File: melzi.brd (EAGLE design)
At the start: 208.3 x 49.5 mm, 130 parts, among them IC2 A4988, IC3 A4988, IC4 A4988, IC5 7805DT, IC6 ATMEGA644A, IC7 4050D, IC8 FT232RL-BASICSSOP, M1 RFP30N06LE, M2 RFP30N06LE, M3 RFP30N06LE, Q1 16MHZ, T2 TRIM, T3 TRIM, T4 TRIM, U2 A4982, X1 MICROSD, X2 MINI-USB-SHIELD-UX60-MB-5ST

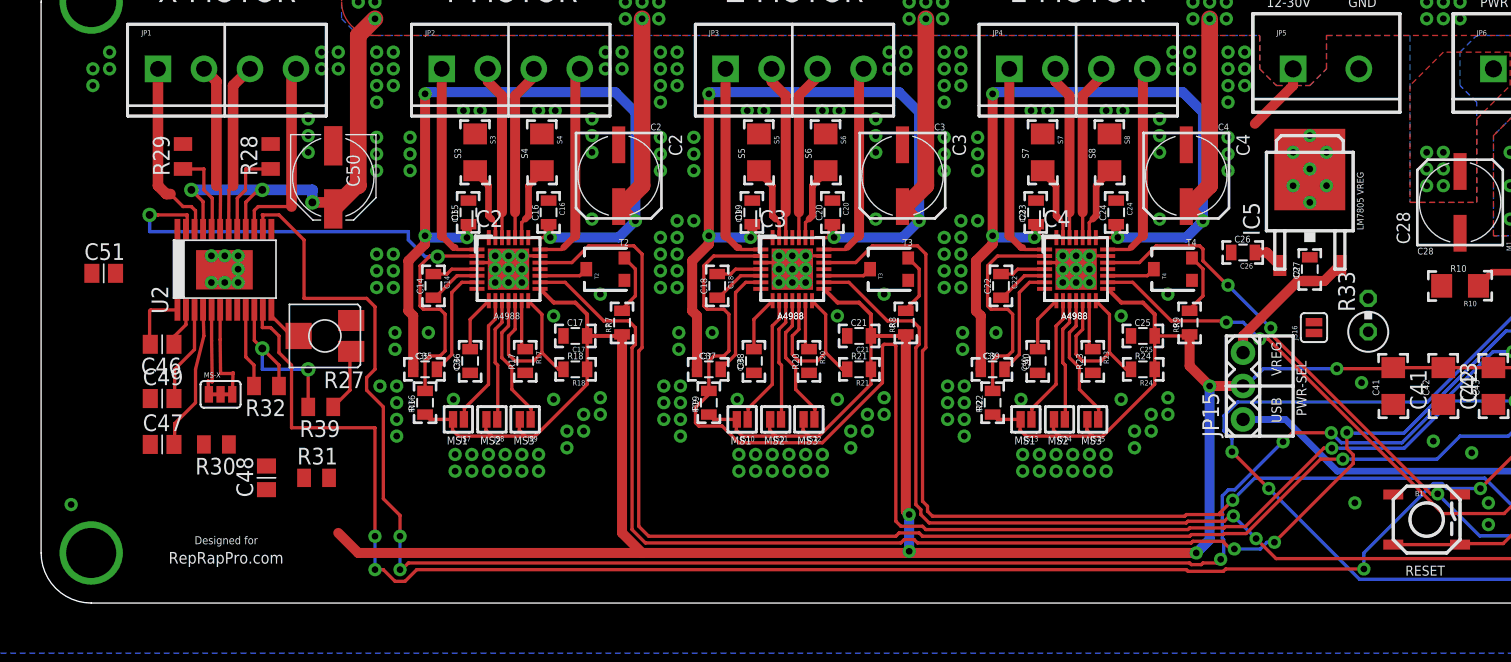
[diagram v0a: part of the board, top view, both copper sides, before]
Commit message: New stepper drivers - X axis done.
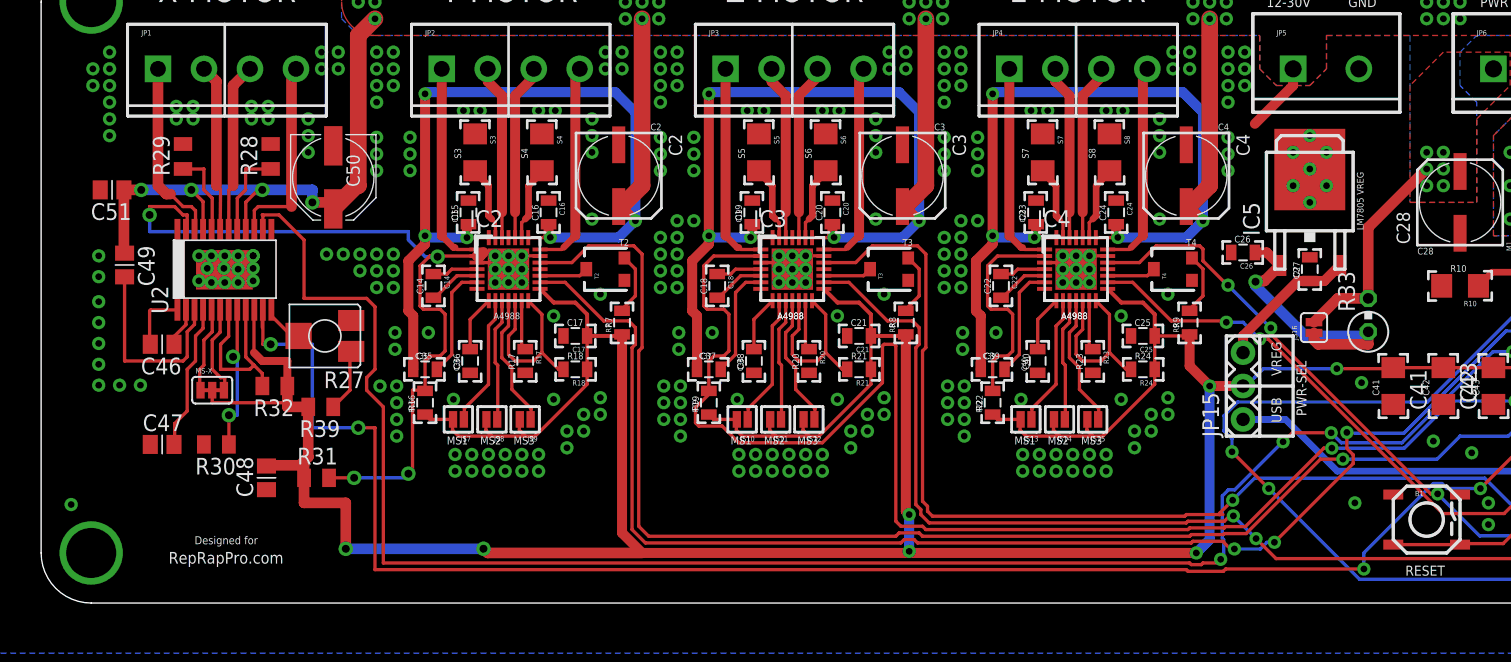
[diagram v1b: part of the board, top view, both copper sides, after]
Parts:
- moved C49 10.6 mm to (6.35, 25.7), turned to 270 degrees
- moved C51 6.38 mm to (5.40, 31.4), turned to 180 degrees
- moved MS-X 0.71 mm to (13.0, 16.2)
- moved R32 0.64 mm to (17.8, 16.5)
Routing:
- net VMOT: track 277.1 -> 303.6 mm, vias 95 -> 96
- net VCC: track 446.0 -> 465.4 mm
- net N$36: track 2.31 -> 21.1 mm, vias 0 -> 1
- net !XYEENABLE: track 62.6 -> 78.1 mm, vias 2 -> 4
- net N$8: track 0.00 -> 11.5 mm, vias 0 -> 2
- net N$10: track 6.05 -> 13.8 mm
- net N$23: track 7.39 -> 15.1 mm
- net X-STEP: track 136.2 -> 137.6 mm
- net N$31: track 7.51 -> 6.96 mm
- net X-DIR: vias 6 -> 4
- net GND: vias 300 -> 333

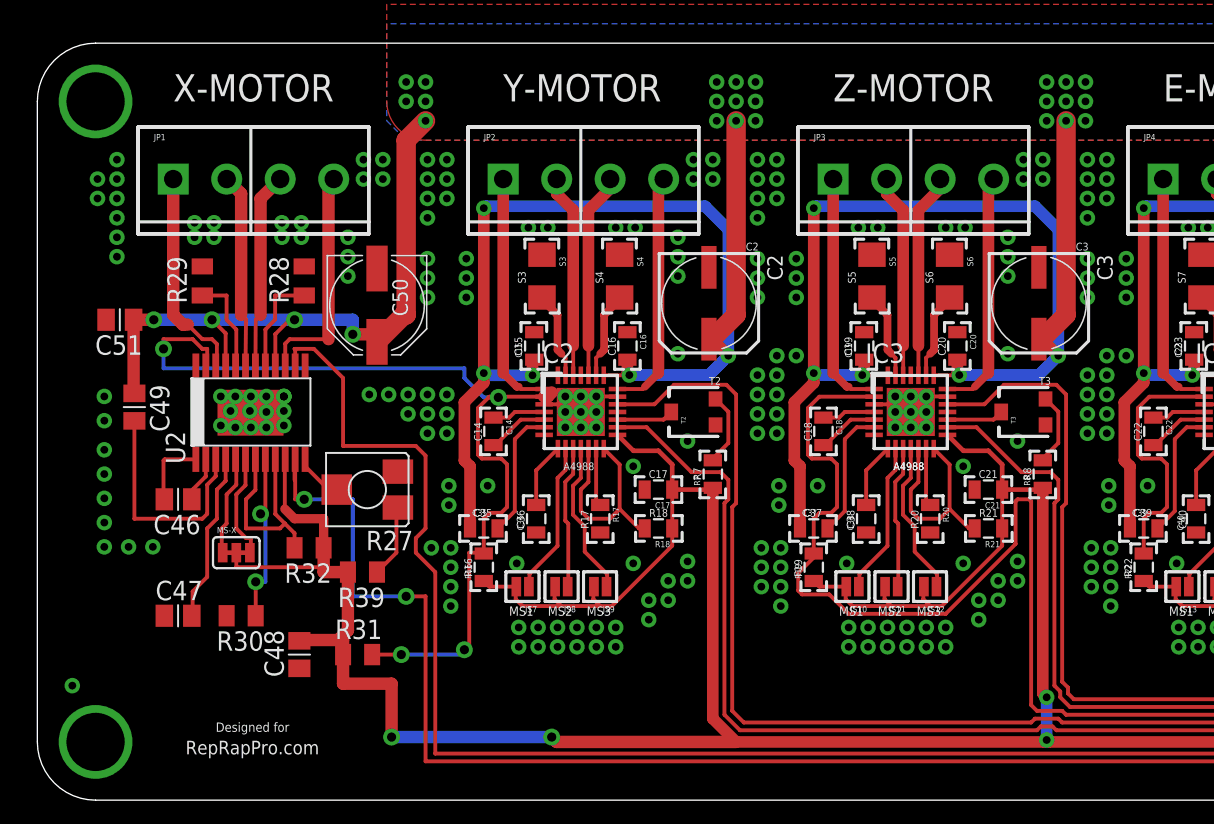
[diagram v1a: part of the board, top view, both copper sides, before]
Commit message: Y and Z drives added.
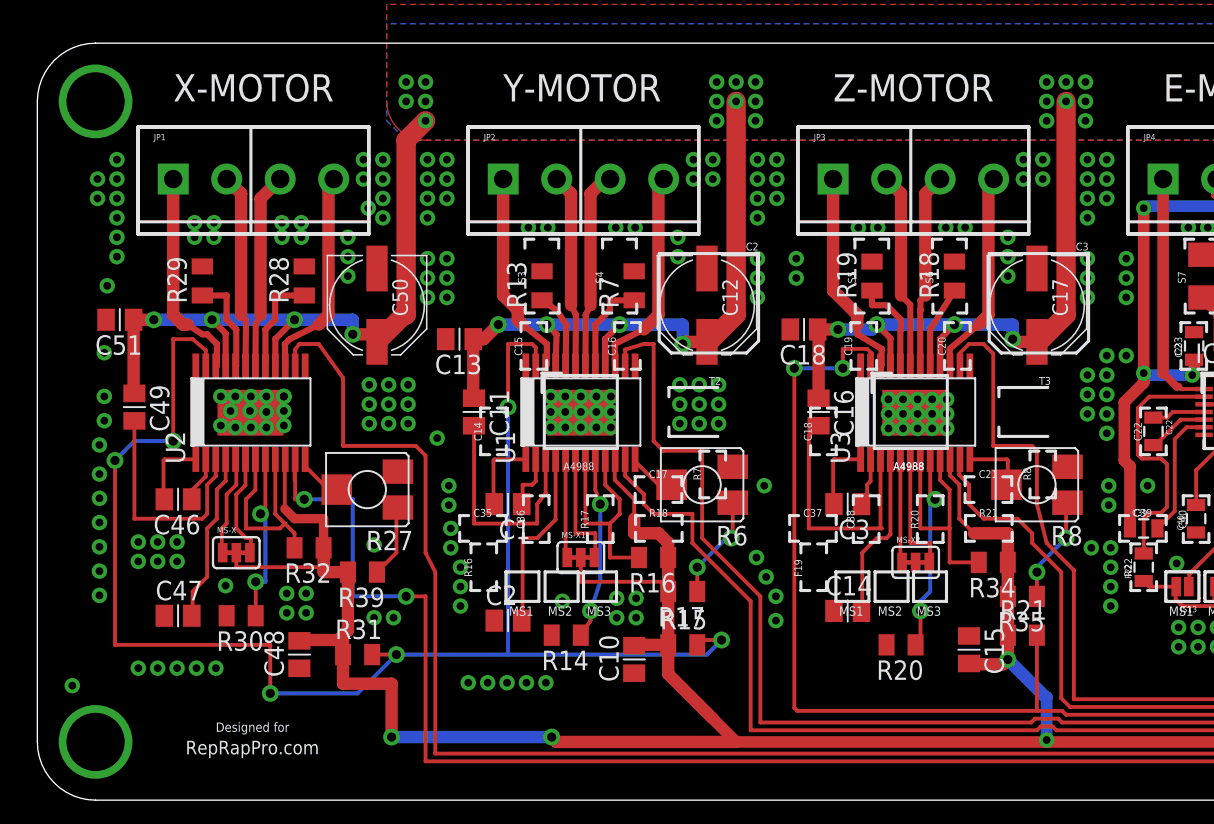
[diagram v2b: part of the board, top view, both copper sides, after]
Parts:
- removed C19, C20, C35, C37: .1uf, SparkFun:0805
- removed C21, C36, C38: .22uf, SparkFun:0805
- removed IC2, IC3: A4988, allegro:QFN28ET
- removed JS10, JS7: MS1, SparkFun:SJ_2S
- removed JS11, JS8: MS2, SparkFun:SJ_2S
- removed JS12, JS9: MS3, SparkFun:SJ_2S
- removed S3, S4, S5, S6: 0.05, SparkFun:1206
- removed T2, T3: TRIM, SparkFun:TRIMPOT-3MM
- added C1, C11, C13: 0.1uF, ipc-7351-capacitor:CAPC2012X145AN
- added C10: 10uF, ipc-7351-capacitor:CAPC2012X145AN
- added C12: 100uF, rcl:PANASONIC_D
- added MS-X1, MS-X2: (no value), printrbot:SJ_3_CONNECTED
- added R13: 0.11, ipc-7351-resistor:RESC2012X70N
- added R14: 10k, ipc-7351-resistor:RESC2012X70N
- added R15, R34: 100k, ipc-7351-resistor:RESC2012X70N
- added R35: 20k, ipc-7351-resistor:RESC2012X70N
- added R6: 10k, printrbot:RTRIM-ST4ETB
- added U1, U3: A4982, printrbot:TSSOP-24
- C14: value .1uf -> 0.22uF; device SparkFun:0805 -> ipc-7351-capacitor:CAPC2012X145AN
- C15: value .1uf -> 10uF; device SparkFun:0805 -> ipc-7351-capacitor:CAPC2012X145AN
- C16, C18: value .1uf -> 0.1uF; device SparkFun:0805 -> ipc-7351-capacitor:CAPC2012X145AN
- C17: value .22uf -> 100uF; device SparkFun:0805 -> rcl:PANASONIC_D
- C2: value 100 uF -> 0.22uF; device rcl:UD-6,3X7,7_NICHICON -> ipc-7351-capacitor:CAPC2012X145AN
- C3: value 100 uF -> 0.1uF; device rcl:UD-6,3X7,7_NICHICON -> ipc-7351-capacitor:CAPC2012X145AN
- R16, R20: device SparkFun:0805 -> ipc-7351-resistor:RESC2012X70N
- R17: value 10k -> 20k; device SparkFun:0805 -> ipc-7351-resistor:RESC2012X70N
- R18: value 10k -> 0.11; device SparkFun:0805 -> ipc-7351-resistor:RESC2012X70N
- R19: value 100k -> 0.11; device SparkFun:0805 -> ipc-7351-resistor:RESC2012X70N
- R21: value 10k -> 100k; device SparkFun:0805 -> ipc-7351-resistor:RESC2012X70N
- R7: value 20k -> 0.11; device SparkFun:0805 -> ipc-7351-resistor:RESC2012X70N
- R8: value 20k -> 10k; device SparkFun:0805 -> printrbot:RTRIM-ST4ETB
- moved C15 34.7 mm to (61.0, 9.84), turned to 270 degrees
- moved C17 27.5 mm to (65.4, 32.4), turned to 270 degrees
- moved C14 26.0 mm to (53.0, 12.4), turned to 0 degrees
- moved R18 25.4 mm to (60.0, 34.3), turned to 90 degrees
- moved C2 24.6 mm to (30.8, 11.7), turned to 0 degrees
- moved R19 19.4 mm to (54.6, 34.3)
- moved C3 18.1 mm to (53.0, 19.4), turned to 180 degrees
- moved R7 13.3 mm to (39.1, 33.7)
- moved C16 13.2 mm to (51.1, 25.4)
- moved R16 11.1 mm to (40.3, 15.9), turned to 180 degrees
- moved R20 8.47 mm to (56.5, 10.2), turned to 180 degrees
- moved R21 7.33 mm to (64.5, 10.8), turned to 0 degrees
- moved R17 7.20 mm to (42.2, 13.7), turned to 180 degrees
- moved C18 6.79 mm to (50.2, 30.8), turned to 180 degrees
- moved R8 0.80 mm to (65.4, 20.6)
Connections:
- removed net XCP3: C14.1, IC2.4
- removed net XCP4: C14.2, IC2.5
- removed net XCP5: C18.1, IC3.4
- removed net XCP6: C18.2, IC3.5
- removed net XREF1: IC2.17, T2.2
- removed net XREF3: R7.2, T2.3
- removed net XREF4: IC3.17, T3.2
- removed net XREF5: R8.2, T3.3
- removed net XROSC1: IC2.13, R17.1
- removed net XROSC2: IC3.13, R20.1
- removed net XSENSE3: IC2.27, S3.2
- removed net XSENSE4: IC2.23, S4.2
- removed net XSENSE5: IC3.27, S5.2
- removed net XSENSE6: IC3.23, S6.2
- removed net XSLEEP1: IC2.12, IC2.14, R18.2
- removed net XSLEEP2: IC3.12, IC3.14, R21.2
- removed net XVCP1: C35.2, IC2.6
- removed net XVCP2: C37.2, IC3.6
- removed net XVREG1: C36.2, IC2.8
- removed net XVREG2: C38.2, IC3.8
- removed net YOUT1A: IC2.24, JP2.3
- removed net YOUT1B: IC2.21, JP2.4
- removed net YOUT2A: IC2.26, JP2.2
- removed net YOUT2B: IC2.1, JP2.1
- removed net ZOUT1A: IC3.24, JP3.3
- removed net ZOUT1B: IC3.21, JP3.4
- removed net ZOUT2A: IC3.26, JP3.2
- removed net ZOUT2B: IC3.1, JP3.1
- new net N$18: R6.W, U1.12
- new net N$19: R14.1, U1.8
- new net N$3: C1.2, U1.1
- new net N$37: C2.2, U1.4
- new net N$38: R16.2, U1.7, U1.9
- new net N$39: C11.2, U1.3
- new net N$40: MS-X1.1, U1.5
- new net N$41: MS-X1.3, U1.6
- new net N$42: JP2.3, U1.18
- new net N$43: JP2.4, U1.15
- new net N$44: JP2.2, U1.19
- new net N$45: JP2.1, U1.22
- new net N$46: R17.1, R6.1
- new net N$47: R19.1, U3.20
- new net N$48: R8.W, U3.12
- new net N$49: R20.1, U3.8
- new net N$50: C14.2, U3.4
- new net N$51: R34.2, U3.7, U3.9
- new net N$52: C16.2, U3.3
- new net N$53: MS-X2.1, U3.5
- new net N$54: MS-X2.3, U3.6
- new net N$55: JP3.3, U3.18
- new net N$56: JP3.4, U3.15
- new net N$57: JP3.2, U3.19
- new net N$58: JP3.1, U3.22
- new net N$59: R35.1, R8.1
- net !XYEENABLE: now also R15.2, U1.23; no longer IC2.2, R16.2
- net !ZENABLE: now also R21.2, U3.23; no longer IC3.2, R19.2
- net GND: now also C10.1, C12.-, C13.2, C14.1, C15.1, C17.-, C18.2, C2.1, R13.2, R14.2, R18.2, R19.2, R6.2, R7.2, R8.2, U1.13, U1.24, U1.PAD, U3.13, U3.24, U3.PAD; no longer C15.2, C16.1, C17.2, C19.2, C2.-, C20.1, C21.2, C3.-, C36.1, C38.1, IC2.18, IC2.20, IC2.25, IC2.3, IC2.7, IC2.EXP, IC3.18, IC3.20, IC3.25, IC3.3, IC3.7, IC3.EXP, R17.2, S3.1, S4.1, S5.1, S6.1, T2.1, T3.1
- net N$11: now also C1.1, U1.2; no longer IC2.10, JS8.1
- net N$16: now also R7.1, U1.17; no longer IC2.11, JS9.1
- net N$17: now also R13.1, U1.20; no longer IC2.9, JS7.1
- net N$20: now also C3.2, U3.1; no longer IC3.9, JS10.1
- net N$21: now also C3.1, U3.2; no longer IC3.10, JS11.1
- net N$22: now also R18.1, U3.17; no longer IC3.11, JS12.1
- net VCC: now also C10.2, C15.2, MS-X1.2, MS-X2.2, R15.1, R17.2, R34.1, R35.2, U1.10, U3.10; no longer C17.1, C21.1, IC2.15, IC3.15, JS10.2, JS11.2, JS12.2, JS7.2, JS8.2, JS9.2, R18.1, R19.1, R7.1, R8.1
- net VMOT: now also C11.1, C12.+, C13.1, C16.1, C17.+, C18.1, U1.16, U1.21, U3.16, U3.21; no longer C15.1, C16.2, C19.1, C2.+, C20.2, C3.+, C35.1, C37.1, IC2.22, IC2.28, IC3.22, IC3.28
- net Y-DIR: now also U1.14; no longer IC2.19
- net Y-STEP: now also U1.11; no longer IC2.16
- net Z-DIR: now also U3.14; no longer IC3.19
- net Z-STEP: now also U3.11; no longer IC3.16
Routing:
- net VMOT: track 303.6 -> 231.5 mm, vias 96 -> 92
- net VCC: track 465.4 -> 427.0 mm
- net !XYEENABLE: track 78.1 -> 114.3 mm, vias 4 -> 6
- net N$52: track 0.00 -> 16.3 mm
- net ZOUT1B: track 16.2 -> 0.00 mm
- net YOUT1B: track 16.2 -> 0.00 mm
- net ZOUT2B: track 15.8 -> 0.00 mm
- net YOUT2B: track 15.8 -> 0.00 mm
- net N$51: track 0.00 -> 15.4 mm
- net N$39: track 0.00 -> 14.9 mm
- net N$38: track 0.00 -> 14.8 mm
- net N$43: track 0.00 -> 14.0 mm
- net XSLEEP1: track 13.8 -> 0.00 mm
- net XSLEEP2: track 13.8 -> 0.00 mm
- net N$58: track 0.00 -> 13.8 mm
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
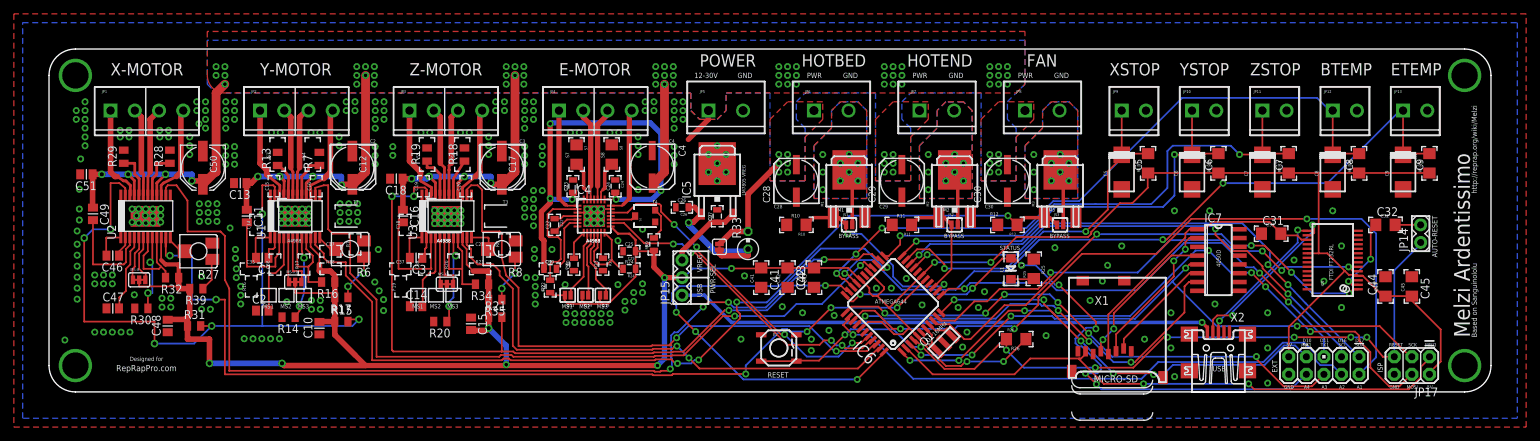
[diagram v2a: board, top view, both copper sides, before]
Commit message: Pretty much finalised.  A couple of unrouted grounds need to be fixed.
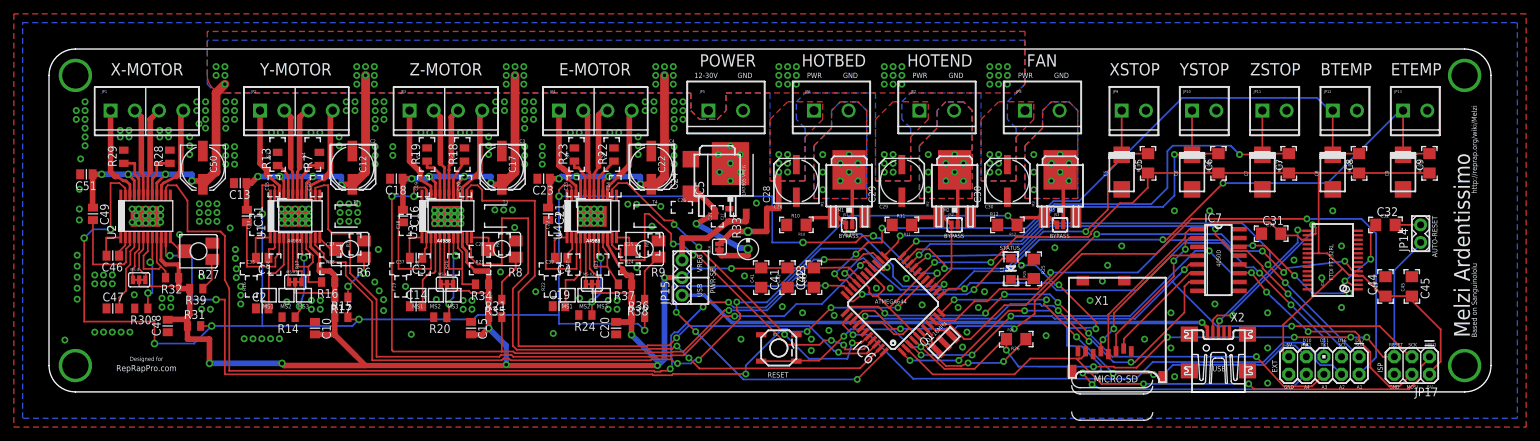
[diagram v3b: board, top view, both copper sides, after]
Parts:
- removed C25, C40: .22uf, SparkFun:0805
- removed C26: .33uf, SparkFun:0805
- removed C39: .1uf, SparkFun:0805
- removed IC4: A4988, allegro:QFN28ET
- removed JS13: MS1, SparkFun:SJ_2S
- removed JS14: MS2, SparkFun:SJ_2S
- removed JS15: MS3, SparkFun:SJ_2S
- removed S7, S8: 0.05, SparkFun:1206
- removed T4: TRIM, SparkFun:TRIMPOT-3MM
- added C19: 0.22uF, ipc-7351-capacitor:CAPC2012X145AN
- added C20: 10uF, ipc-7351-capacitor:CAPC2012X145AN
- added C21: 0.1uF, ipc-7351-capacitor:CAPC2012X145AN
- added MS-X3: (no value), printrbot:SJ_3_CONNECTED
- added R36: 100k, ipc-7351-resistor:RESC2012X70N
- added R37: 4k7, ipc-7351-resistor:RESC2012X70N
- added R38: 20k, ipc-7351-resistor:RESC2012X70N
- added U4: A4982, printrbot:TSSOP-24
- C22: value .1uf -> 100uF; device SparkFun:0805 -> rcl:PANASONIC_D
- C23: value .1uf -> 0.1uF; device SparkFun:0805 -> ipc-7351-capacitor:CAPC2012X145AN
- C24: value .1uf -> 4.7 uF; device SparkFun:0805 -> rcl:SMC_C
- C4: value 100 uF -> 0.1uF; device rcl:UD-6,3X7,7_NICHICON -> ipc-7351-capacitor:CAPC2012X145AN
- IC6: value ATMEGA644A -> ATMEGA1284P
- R16, R32, R34: value 100k -> 4k7
- R22: value 100k -> 0.11; device SparkFun:0805 -> ipc-7351-resistor:RESC2012X70N
- R23: value 10k -> 0.11; device SparkFun:0805 -> ipc-7351-resistor:RESC2012X70N
- R24: device SparkFun:0805 -> ipc-7351-resistor:RESC2012X70N
- R9: value 20k -> 10k; device SparkFun:0805 -> printrbot:RTRIM-ST4ETB
- moved R22 21.2 mm to (81.6, 34.3)
- moved C4 18.6 mm to (74.0, 19.4), turned to 180 degrees
- moved R23 16.4 mm to (75.9, 34.3), turned to 90 degrees
- moved C22 16.2 mm to (87.0, 32.4)
- moved C24 11.0 mm to (92.7, 31.1), turned to 90 degrees
- moved R24 9.21 mm to (77.5, 11.1)
- moved C23 4.39 mm to (71.4, 30.8), turned to 180 degrees
- moved IC5 1.91 mm to (98.4, 30.5)
- moved C27 1.75 mm to (98.3, 25.6)
- moved R9 1.51 mm to (86.0, 20.6)
- moved C10 0.64 mm to (38.4, 9.21), turned to 270 degrees
- moved C15 0.63 mm to (61.0, 9.21)
- moved R15 0.63 mm to (42.2, 10.8)
- moved R20 0.63 mm to (56.5, 10.8)
- moved C2 0.32 mm to (30.8, 12.1)
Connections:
- removed net EOUT1A: IC4.24, JP4.3
- removed net EOUT1B: IC4.21, JP4.4
- removed net EOUT2A: IC4.26, JP4.2
- removed net EOUT2B: IC4.1, JP4.1
- removed net N$24: IC4.10, JS14.1
- removed net XCP7: C22.1, IC4.4
- removed net XCP8: C22.2, IC4.5
- removed net XREF6: IC4.17, T4.2
- removed net XREF7: R9.2, T4.3
- removed net XROSC3: IC4.13, R23.1
- removed net XSENSE7: IC4.27, S7.2
- removed net XSENSE8: IC4.23, S8.2
- removed net XSLEEP3: IC4.12, IC4.14, R24.2
- removed net XVCP3: C39.2, IC4.6
- removed net XVREG3: C40.2, IC4.8
- new net N$60: R22.1, U4.17
- new net N$61: R23.1, U4.20
- new net N$62: R9.W, U4.12
- new net N$63: R24.1, U4.8
- new net N$64: C19.2, U4.4
- new net N$65: R37.2, U4.7, U4.9
- new net N$66: C21.2, U4.3
- new net N$67: MS-X3.1, U4.5
- new net N$68: MS-X3.3, U4.6
- new net N$70: JP4.3, U4.18
- new net N$71: JP4.4, U4.15
- new net N$72: JP4.2, U4.19
- new net N$73: JP4.1, U4.22
- new net N$74: R38.1, R9.1
- net !XYEENABLE: now also R36.2, U4.23; no longer IC4.2, R22.2
- net E-DIR: now also U4.14; no longer IC4.19
- net E-STEP: now also U4.11; no longer IC4.16
- net GND: now also C19.1, C20.1, C22.-, C24.-, R22.2, R24.2, R9.2, U4.13, U4.24, U4.PAD; no longer C24.1, C25.2, C26.2, C4.-, C40.1, IC4.18, IC4.20, IC4.25, IC4.3, IC4.7, IC4.EXP, S7.1, S8.1, T4.1
- net N$25: now also C4.2, U4.1; no longer IC4.11, JS15.1
- net N$27: now also C4.1, U4.2; no longer IC4.9, JS13.1
- net N$36: now also C24.+; no longer C26.1
- net VCC: now also C20.2, MS-X3.2, R36.1, R37.1, R38.2, U4.10; no longer C25.1, IC4.15, JS13.2, JS14.2, JS15.2, R22.1, R24.1, R9.1
- net VMOT: now also C21.1, C22.+, U4.16, U4.21; no longer C24.2, C39.1, C4.+, IC4.22, IC4.28
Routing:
- net !XYEENABLE: track 114.3 -> 230.1 mm, vias 6 -> 11
- net VMOT: track 231.5 -> 191.8 mm, vias 92 -> 90
- net Z-STEP: track 75.8 -> 93.9 mm
- net VCC: track 427.0 -> 444.5 mm, vias 11 -> 12
- net N$66: track 0.00 -> 16.2 mm
- net EOUT1B: track 16.2 -> 0.00 mm
- net EOUT2B: track 15.8 -> 0.00 mm
- net XSLEEP3: track 13.8 -> 0.00 mm
- net N$71: track 0.00 -> 13.7 mm
- net N$73: track 0.00 -> 13.5 mm
- net N$65: track 0.00 -> 13.5 mm
- net EOUT1A: track 13.4 -> 0.00 mm
- net N$70: track 0.00 -> 13.4 mm
- net EOUT2A: track 13.3 -> 0.00 mm
- net N$72: track 0.00 -> 12.6 mm
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
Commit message: Melzi 2.0 finished (e&oe...)
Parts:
- JP4: value Y-MOT -> E-MOT
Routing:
- net N$7: track 2.16 -> 3.60 mm
- net VMOT: track 191.8 -> 192.4 mm
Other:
- board text added: "+"
- board text added: "-"
- board text added: "E motor"
- board text added: "X motor"
- board text added: "Y motor"
- board text added: "Z motor"
- board text added: "bed"
- board text added: "btemp"
- board text added: "etemp"
- board text added: "fan"
- board text added: "hot end"
- board text added: "power"
- board text added: "reprappro.com RepRap Melzi V2.0 Licence: GPL"
- board text added: "x-stop"
- board text added: "y-stop"
- board text added: "z-stop"
